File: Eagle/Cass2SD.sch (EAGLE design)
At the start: 34 parts, among them IC1 LM358N, Q1 8MHz, Q2 BC557C, Q3 BC447, Q4 BC447, SW1 EC12E_SW, U1 ATMEGA328P-PU, U3 MCP1702-5002, X1 MAB5SH

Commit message: Eagle files updated/added
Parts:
- removed C11, C12: 22p, resistor:C-EU050-025X075
- removed DIS1: TUXGR_16X2_R2, display-lcd:TUXGR_16X2_R2
- removed JP4: (no value), pinhead:PINHD-1X2
- removed LED1: (no value), led:LED5MM
- removed Q2: BC557C, transistor-pnp:BC557C
- removed Q3, Q4: BC447, transistor-npn:BC447
- removed R14: 270, resistor:R-EU_0309/12
- removed R17: 10k, resistor:R-EU_M1206
- removed R18: 33k, resistor:R-EU_M1206
- removed R19: 3k3, resistor:R-EU_M1206
- removed R20: 100k, resistor:R-EU_M1206
- removed R21: 27k, resistor:R-EU_M1206
- removed R22: (no value), resistor:R-EU_M1206
- removed SV2: (no value), con-lstb:MA06-1
- removed U1: ATMEGA328P-PU, Atmel_By_element14_Batch_1-00:ATMEGA328P-PU
- removed U3: MCP1702-5002, AdditionalSymbols:MCP1702
- added ADP1: SODIAL_MICROSD_SPI_ADAPTER, BerndAdditionalSymbols:SODIAL_MICROSD_SPI_ADAPTER
- added C8: 10µ, resistor:CPOL-EUE2.5-7
- added C9: 100n, resistor:C-EU050-025X075
- added D2, D3: 1N4148DO35-7, diode:1N4148DO35-7
- added IC2: ATMEGA328P-PU, BerndAdditionalSymbols:ATMEGA328P-PU
- added IC3: LM358N, linear:LM358N
- added JP1: PWR, pinhead:PINHD-1X2
- added JP2: ISP, pinhead:PINHD-2X3
- added LCD1: LCD_2X16, BerndAdditionalSymbols:LCD_2X16
- added R1, R4: 10k, resistor:R-EU_0207/10
- added R2: 68k, resistor:R-EU_0207/10
- added R3: 33k, resistor:R-EU_0207/10
- added R5: 10k, resistor:R-TRIMM64P
- added R6: 1M, resistor:R-EU_0207/10
- added R9: 100k, resistor:R-EU_0207/10
- C1: value 1n -> 10µ; device resistor:C-EU050-025X075 -> resistor:CPOL-EUE2.5-7
- C10: value 10µ -> 560p; device resistor:CPOL-EUE10-20 -> resistor:C-EU050-025X075
- C2: value 10n -> 100n
- C4, C5: value 100n -> 22p
- C7: value 10µ -> 100n; device resistor:CPOL-EUE10-20 -> resistor:C-EU050-025X075
- IC1: value LM358N -> MCP1702-5002; device linear:LM358N -> AdditionalSymbols:MCP1702
- JP3: value (none) -> CABEL_TYPE; device pinhead:PINHD-2X3 -> jumper:JP3Q
- R7: value 10k -> 15R; device resistor:R-TRIMM64P -> resistor:R-EU_0207/10
- R8: value 10k -> 270; device resistor:R-EU_0309/12 -> resistor:R-EU_0207/10
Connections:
- removed net +12V: C5.1, C7.+, Q2.C, U3.IN
- removed net N$15: DIS1.CONTR, R7.S
- removed net N$19: D1.A, JP4.1
- removed net N$21: D1.C, Q2.E, R18.2
- removed net N$22: JP3.5, R17.1, U1.PC6
- removed net N$23: Q2.B, R18.1, R19.2
- removed net N$24: LED1.A, R19.1, SW1G$2.2
- removed net N$25: LED1.C, Q3.C
- removed net N$26: C2.1, Q3.B, R20.2, R21.2
- removed net N$27: U1.PD6
- removed net N$28: Q4.C, R22.1, U1.PD7
- removed net N$29: Q4.B, SW1G$2.1
- removed net PD0: DIS1.D4, U1.PD0
- removed net PD1: DIS1.D5, U1.PD1
- removed net PD2: DIS1.D6, U1.PD2
- removed net PD3: DIS1.D7, U1.PD3
- removed net PD4: DIS1.RS, U1.PD4
- removed net PD5: DIS1.E, U1.PD5
- new net CS: ADP1.CS, IC2.PB2
- new net LCD_D4: IC2.PC0, LCD1.DB4
- new net LCD_D5: IC2.PC1, LCD1.DB5
- new net LCD_D6: IC2.PC2, LCD1.DB6
- new net LCD_D7: IC2.PC3, LCD1.DB7
- new net LCD_E: IC2.PD7, LCD1.E
- new net LCD_RS: IC2.PD5, LCD1.RS
- new net LCD_RW: IC2.PD6, LCD1.R/W
- new net MISO: ADP1.MISO, IC2.PB4, JP2.1
- new net MOSI: ADP1.MOSI, IC2.PB3, JP2.4
- new net N$1: C1.+, C2.1, D1.C, IC1.IN
- new net N$16: JP3.4, X1.1
- new net N$2: C10.1, C9.2, D2.C, D3.A, IC3A.-IN, R9.2
- new net N$3: IC3B.+IN, R2.1, R3.2
- new net N$7: IC3A.+IN, R6.1, R7.2
- new net N$8: IC2.PD2, IC3A.OUT, R6.2
- new net N$9: D1.A, JP1.2
- new net RESET: IC2.PC6, JP2.5, R1.1
- new net ROTARY_A: IC2.PC4, SW1G$1.A
- new net ROTARY_B: IC2.PC5, SW1G$1.B
- new net SCK: ADP1.SCK, IC2.PB5, JP2.3
- new net SELECT_KEY: IC2.PB0, SW1G$2.2
- new net VIRTUAL_GND: C10.2, D2.A, D3.C, IC3B.-IN, IC3B.OUT, R7.1, R9.1
- net +5V: now also ADP1.VCC, C7.1, C8.+, IC1.OUT, IC2.AVCC, IC2.VCC, IC3P.V+, JP2.2, LCD1.VCC, R1.2, R2.2, R4.2; no longer C10.+, C4.1, DIS1.VCC, JP3.2, R14.2, R17.2, R22.2, U1.AVCC, U1.VCC, U3.OUT
- net GND: now also ADP1.GND, C1.-, C7.2, C8.-, IC1.GND, IC2.GND, IC2.GND_2, IC3P.V-, JP1.1, JP2.6, LCD1.LEDK, LCD1.VSS, R3.1, R5.E, SW1G$2.1, X1.2, X1.PE; no longer C1.2, C10.-, C11.2, C12.2, C7.-, DIS1.GND, DIS1.NC@2, DIS1.R/W, JP3.6, JP4.2, Q3.E, Q4.E, R20.1, R7.A, U1.GND, U1.GND_2, U3.GND
- net N$10: now also IC2.PD1, JP3.5, JP3.6; no longer JP3.4, U1.PB3
- net N$11: now also LCD1.LEDA, R8.1; no longer JP3.1, U1.PB4
- net N$12: now also X1.3; no longer U1.PB5
- net N$13: now also LCD1.VO, R5.S; no longer DIS1.NC@1, R14.1
- net N$14: now also R4.1, R5.A; no longer R7.E, R8.1
- net N$4: now also C4.1, IC2.PB6; no longer C11.1, U1.PB6
- net N$5: now also C5.1, IC2.PB7; no longer C12.1, U1.PB7
- net N$6: now also C9.1, JP3.1, JP3.2; no longer C1.1, U1.AREF
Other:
- note added: "Autor:"
- note added: "Projekt:"
- note added: "Version:"
- moved on the sheet: C2, C3, C4, C5, C6, D1, Q1, R8, SW1, X1

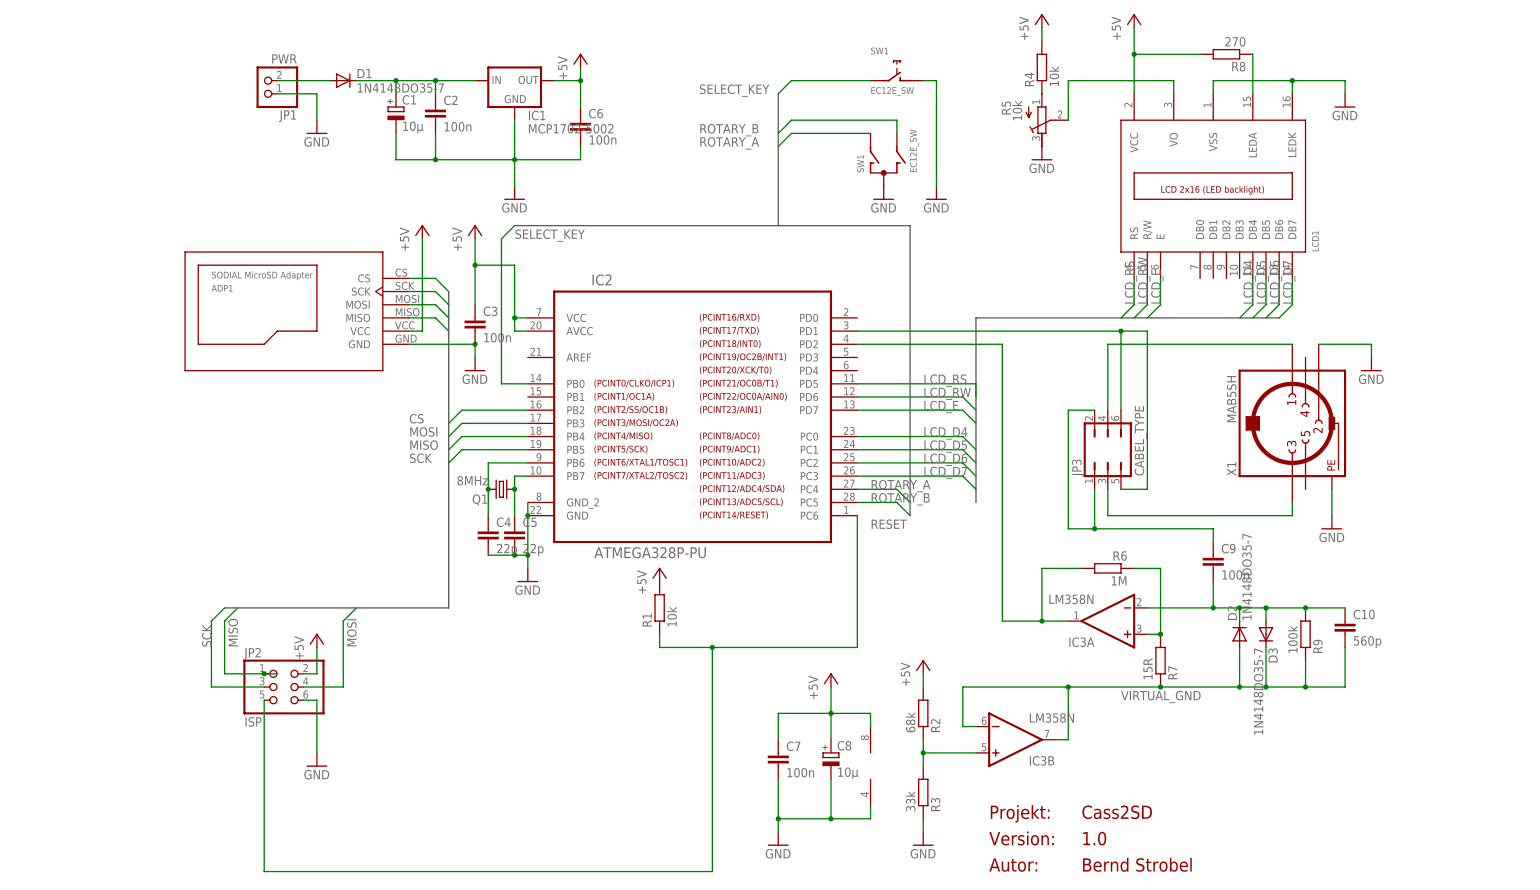
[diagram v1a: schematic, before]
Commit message: Changed to external XTAL with 16MHz
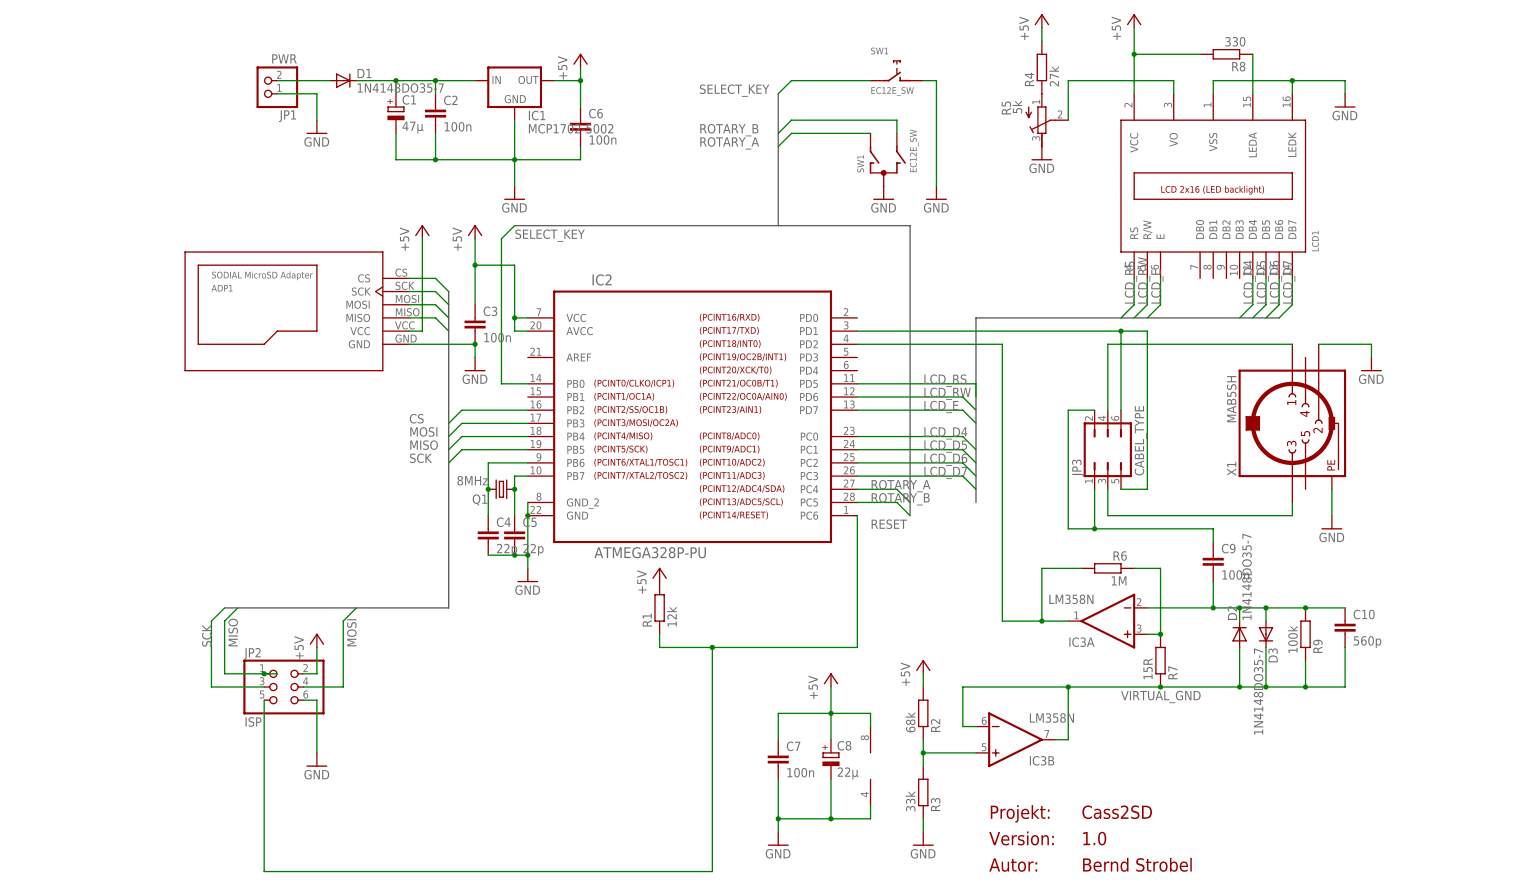
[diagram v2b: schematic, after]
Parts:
- C1: value 10µ -> 47µ
- C8: value 10µ -> 22µ
- R1: value 10k -> 12k
- R4: value 10k -> 27k
- R5: value 10k -> 5k
- R8: value 270 -> 330
